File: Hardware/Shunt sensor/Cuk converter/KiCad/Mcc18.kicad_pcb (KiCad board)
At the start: 2 copper layers, 199.1 x 107.2 mm, 60 parts, among them Q1 IRFP4321PbF, U1 INA240, U2 DRIVER_(INEP), U3 LM7812_TO220, U4 Signals_MCC, U5 ZCS, U6 INA211_DCK_6

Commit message: finished the first version
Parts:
- removed C_INA211, C_INA240: 100n, MCCplaca:C_0805_2012Metric_Pad1.29x1.40mm_HandSolder
- removed RShunt1: R, MCCplaca Shunt:PML100HZPJV0L5
- removed R_Ina211_Ref1, R_Ina211_SIG1, R_Ina240_REF1, R_Ina240_SIG1: ??, MCCplaca Shunt:R_0805_2012Metric_Pad1.29x1.40mm_HandSolder
- added C1: 100nF, MCCplaca Shunt:C_0805_2012Metric_Pad1.29x1.40mm_HandSolder, B.Cu at (100.8, 51.3)
- added C12: 100nF, MCCplaca Shunt:C_0805_2012Metric_Pad1.29x1.40mm_HandSolder, F.Cu at (119.1, 56.4)
- added R105: 0R, Jumper:SolderJumper-2_P1.3mm_Open_Pad1.0x1.5mm, F.Cu at (126.2, 64.3)
- added R106: 0R, Jumper:SolderJumper-2_P1.3mm_Open_Pad1.0x1.5mm, B.Cu at (115.6, 51.6)
- added R108: 0R, Jumper:SolderJumper-2_P1.3mm_Open_Pad1.0x1.5mm, B.Cu at (115.6, 49.0)
- added R109: ??, Resistor_SMD:R_0805_2012Metric_Pad1.29x1.40mm_HandSolder, B.Cu at (103.9, 50.3)
- added R110: ??, Resistor_SMD:R_0805_2012Metric_Pad1.29x1.40mm_HandSolder, B.Cu at (103.9, 52.6)
- added Rshunt1: 500uR, MCCplaca Shunt:PML100HZPJV0L5, B.Cu at (126.0, 56.6)
- C11: value 10uF -> 100nF; footprint MCCplaca:C_0805_2012Metric_Pad1.29x1.40mm_HandSolder -> MCCplaca Shunt:C_0805_2012Metric_Pad1.29x1.40mm_HandSolder; moved to B.Cu
- R107: value 1R -> 0R; footprint Resistor_SMD:R_0805_2012Metric_Pad1.29x1.40mm_HandSolder -> Jumper:SolderJumper-2_P1.3mm_Open_Pad1.0x1.5mm
- U6: value INA211_DCK_6 -> INA211; moved to B.Cu
- moved U6 42.0 mm to (118.9, 56.4)
- moved C11 40.9 mm to (136.7, 56.9)
- moved R107 29.9 mm to (126.2, 61.7)
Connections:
- net /Shunt+ renamed /Rs+
- C11 pad 2: /Ipanel_adc+ -> +5VA
- R107 pad 1: /Ipanel_SIG -> GNDA
- R107 pad 2: /Ipanel_adc+ -> /Ip_sen-
- U1 pad 2: GND -> GNDA
- U1 pad 3: /Ina240_REF -> GNDA
- U1 pad 4: Net-(U1-Pad4) -> GNDA
- U1 pad 5: Net-(R_Ina240_SIG1-Pad2) -> /INA240_OUT
- U1 pad 6: +5V -> +5VA
- U1 pad 7: /Ina240_REF -> GNDA
- U6 pad 1: Net-(R_Ina211_Ref1-Pad2) -> GNDA
- U6 pad 2: GND -> GNDA
- U6 pad 3: +5V -> +5VA
- U6 pad 6: Net-(R_Ina211_SIG1-Pad2) -> /INA211_OUT
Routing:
- net GNDA: track 47.7 -> 135.8 mm, vias 3 -> 10
- net +5VA: track 7.91 -> 82.1 mm, vias 0 -> 4
- net +5V: track 195.2 -> 139.7 mm, vias 3 -> 1
- net /Ip_sen-: track 0.00 -> 37.5 mm, vias 0 -> 1
- net /Ip_sen+: track 0.00 -> 35.9 mm, vias 0 -> 1
- net /Ipanel_SIG: track 34.1 -> 0.00 mm, vias 2 -> 0
- net /Ina240_REF: track 21.7 -> 0.00 mm, vias 2 -> 0
- net GND: track 271.8 -> 252.6 mm, vias 10 -> 7
- net /-Vp: track 121.6 -> 136.1 mm
- net /Rs+: track 18.9 -> 30.8 mm
- net /INA211_OUT: track 0.00 -> 11.7 mm, vias 0 -> 2
- net Net-(R_Ina240_SIG1-Pad2): track 11.1 -> 0.00 mm, vias 1 -> 0
- net /INA240_OUT: track 0.00 -> 10.4 mm, vias 0 -> 1
- net /Ipanel_adc+: track 5.45 -> 14.9 mm, vias 0 -> 2
- removed copper zone on B.Cu, net (none)
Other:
- net class INA added: clearance 0.3048, trace_width 0.3429, via_dia 0.9, via_drill 0.7
- rule trace_min: 0.508 -> 0.3429

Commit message: fixed clearance
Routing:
- net GNDA: track 135.8 -> 136.4 mm
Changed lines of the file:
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@@
     (thickness 1.6)
     (drawings 8)
-    (tracks 655)
+    (tracks 658)
     (zones 0)
     (modules 61)
@@
     (user_trace_width 9)
     (trace_clearance 0.3048)
-    (zone_clearance 0.3048)
+    (zone_clearance 1.27)
     (zone_45_only no)
     (trace_min 0.3429)
@@
   (segment (start 133.223 54.00804) (end 133.223 51.943) (width 0.508) (layer B.Cu) (net 25))
   (segment (start 133.223 51.943) (end 133.096 51.816) (width 0.508) (layer B.Cu) (net 25))
-  (via (at 130.556 61.633997) (size 1.7) (drill 0.6) (layers F.Cu B.Cu) (net 25))
-  (segment (start 130.556 62.23) (end 130.556 61.633997) (width 0.508) (layer F.Cu) (net 25))
-  (segment (start 131.953 60.236997) (end 131.953 59.40804) (width 0.508) (layer B.Cu) (net 25))
-  (segment (start 130.556 61.633997) (end 131.953 60.236997) (width 0.508) (layer B.Cu) (net 25))
-  (segment (start 131.826 60.363997) (end 130.556 61.633997) (width 0.508) (layer F.Cu) (net 25))
-  (segment (start 131.826 56.896) (end 131.826 60.363997) (width 0.508) (layer F.Cu) (net 25))
-  (segment (start 133.096 51.816) (end 133.096 55.626) (width 0.508) (layer F.Cu) (net 25))
-  (segment (start 133.096 55.626) (end 131.826 56.896) (width 0.508) (layer F.Cu) (net 25))
-  (segment (start 130.467997 61.722) (end 130.556 61.633997) (width 0.508) (layer F.Cu) (net 25))
-  (segment (start 126.888 61.722) (end 130.467997 61.722) (width 0.508) (layer F.Cu) (net 25))
   (via (at 98.806 50.292) (size 1.8) (drill 0.7) (layers F.Cu B.Cu) (net 25))
   (segment (start 101.1405 50.292) (end 99.314 50.292) (width 0.508) (layer B.Cu) (net 25))
@@
   (segment (start 116.22 49.022) (end 117.094 49.022) (width 0.508) (layer B.Cu) (net 25))
   (segment (start 117.094 49.022) (end 119.888 51.816) (width 0.508) (layer B.Cu) (net 25))
+  (via (at 131.445006 61.468) (size 1.7) (drill 0.6) (layers F.Cu B.Cu) (net 25))
+  (segment (start 131.953 60.960006) (end 131.445006 61.468) (width 0.508) (layer B.Cu) (net 25))
+  (segment (start 130.556 62.23) (end 131.318 61.468) (width 0.508) (layer F.Cu) (net 25))
+  (segment (start 131.953 59.40804) (end 131.953 60.960006) (width 0.508) (layer B.Cu) (net 25))
+  (segment (start 131.191006 61.722) (end 131.445006 61.468) (width 0.508) (layer F.Cu) (net 25))
+  (segment (start 126.888 61.722) (end 131.191006 61.722) (width 0.508) (layer F.Cu) (net 25))
+  (segment (start 131.318 61.468) (end 131.445006 61.468) (width 0.508) (layer F.Cu) (net 25))
+  (segment (start 131.953 60.960006) (end 131.445006 61.468) (width 0.508) (layer F.Cu) (net 25))
+  (segment (start 131.953 57.3405) (end 131.953 60.960006) (width 0.508) (layer F.Cu) (net 25))
+  (segment (start 133.1595 56.134) (end 131.953 57.3405) (width 0.508) (layer F.Cu) (net 25))
+  (segment (start 133.096 51.816) (end 133.1595 51.8795) (width 0.508) (layer F.Cu) (net 25))
+  (segment (start 133.1595 51.8795) (end 133.1595 56.134) (width 0.508) (layer F.Cu) (net 25))
   (segment (start 119.94515 57.037999) (end 120.3579 57.037999) (width 0.3429) (layer B.Cu) (net 26))
   (segment (start 118.1585 56.388) (end 118.1585 56.4365) (width 0.3429) (layer F.Cu) (net 26))
@@
   (segment (start 114.3 62.738) (end 115.316 63.754) (width 0.508) (layer F.Cu) (net 60))
   (segment (start 115.316 63.754) (end 125.42521 63.754) (width 0.508) (layer F.Cu) (net 60))
-  (via (at 130.302 64.262) (size 1.7) (drill 0.6) (layers F.Cu B.Cu) (net 61))
-  (segment (start 126.888 64.262) (end 130.302 64.262) (width 0.508) (layer F.Cu) (net 61))
-  (segment (start 134.493 60.69104) (end 134.493 59.40804) (width 0.508) (layer B.Cu) (net 61))
-  (segment (start 130.302 64.262) (end 130.92204 64.262) (width 0.508) (layer B.Cu) (net 61))
-  (segment (start 130.92204 64.262) (end 134.493 60.69104) (width 0.508) (layer B.Cu) (net 61))
+  (via (at 131.445 64.0715) (size 1.7) (drill 0.6) (layers F.Cu B.Cu) (net 61))
+  (segment (start 126.888 64.262) (end 131.2545 64.262) (width 0.508) (layer F.Cu) (net 61))
+  (segment (start 131.2545 64.262) (end 131.445 64.0715) (width 0.508) (layer F.Cu) (net 61))
+  (segment (start 134.493 59.40804) (end 134.493 61.0235) (width 0.508) (layer B.Cu) (net 61))
+  (segment (start 134.493 61.0235) (end 132.294999 63.221501) (width 0.508) (layer B.Cu) (net 61))
+  (segment (start 132.294999 63.221501) (end 131.445 64.0715) (width 0.508) (layer B.Cu) (net 61))
   (via (at 117.856 54.356002) (size 1.5) (drill 0.6) (layers F.Cu B.Cu) (net 62))
   (segment (start 117.8941 54.394102) (end 117.856 54.356002) (width 0.3429) (layer B.Cu) (net 62))
@@
   )
   (zone (net 63) (net_name /Rs+) (layer B.Cu) (hatch full 0.508)
-    (priority 26)
-    (connect_pads yes (clearance 0.3048))
-    (min_thickness 0.254)
+    (priority 6)
+    (connect_pads yes (clearance 1.27))
+    (min_thickness 0.508)
     (fill yes (arc_segments 16) (thermal_gap 0.3048) (thermal_bridge_width 0.3048) (smoothing fillet) (radius 2))
     (polygon
@@
   )
   (zone (net 25) (net_name GNDA) (layer B.Cu) (hatch full 0.508)
-    (priority 25)
+    (priority 5)
     (connect_pads yes (clearance 0.3048))
     (min_thickness 0.508)
@@
   )
   (zone (net 25) (net_name GNDA) (layer F.Cu) (hatch full 0.508)
-    (priority 25)
+    (priority 5)
     (connect_pads yes (clearance 0.3048))
     (min_thickness 0.508)
@@
   )
   (zone (net 46) (net_name /-Vp) (layer B.Cu) (hatch edge 0.508)
-    (priority 3)
+    (priority 6)
     (connect_pads yes (clearance 1.27))
     (min_thickness 0.508)
-    (fill yes (arc_segments 16) (thermal_gap 0.508) (thermal_bridge_width 0.508) (smoothing fillet) (radius 4))
+    (fill yes (arc_segments 16) (thermal_gap 0.508) (thermal_bridge_width 0.508) (smoothing chamfer) (radius 3.81))
     (polygon
       (pts
@@
       )
     )
+  )
+  (zone (net 0) (net_name "") (layer B.Cu) (hatch full 0.508)
+    (connect_pads yes (clearance 0.3048))
+    (min_thickness 0.508)
+    (keepout (tracks allowed) (vias allowed) (copperpour not_allowed))
+    (fill (arc_segments 16) (thermal_gap 0.508) (thermal_bridge_width 0.508) (smoothing chamfer) (radius 2))
+    (polygon
+      (pts
+        (xy 129.4765 55.8165) (xy 129.4765 56.261) (xy 129.4765 57.2135) (xy 129.4765 57.404) (xy 129.4765 57.4675)
+        (xy 122.682 57.4675) (xy 122.682 57.15) (xy 122.682 56.3245) (xy 122.682 55.8165)
+      )
+    )

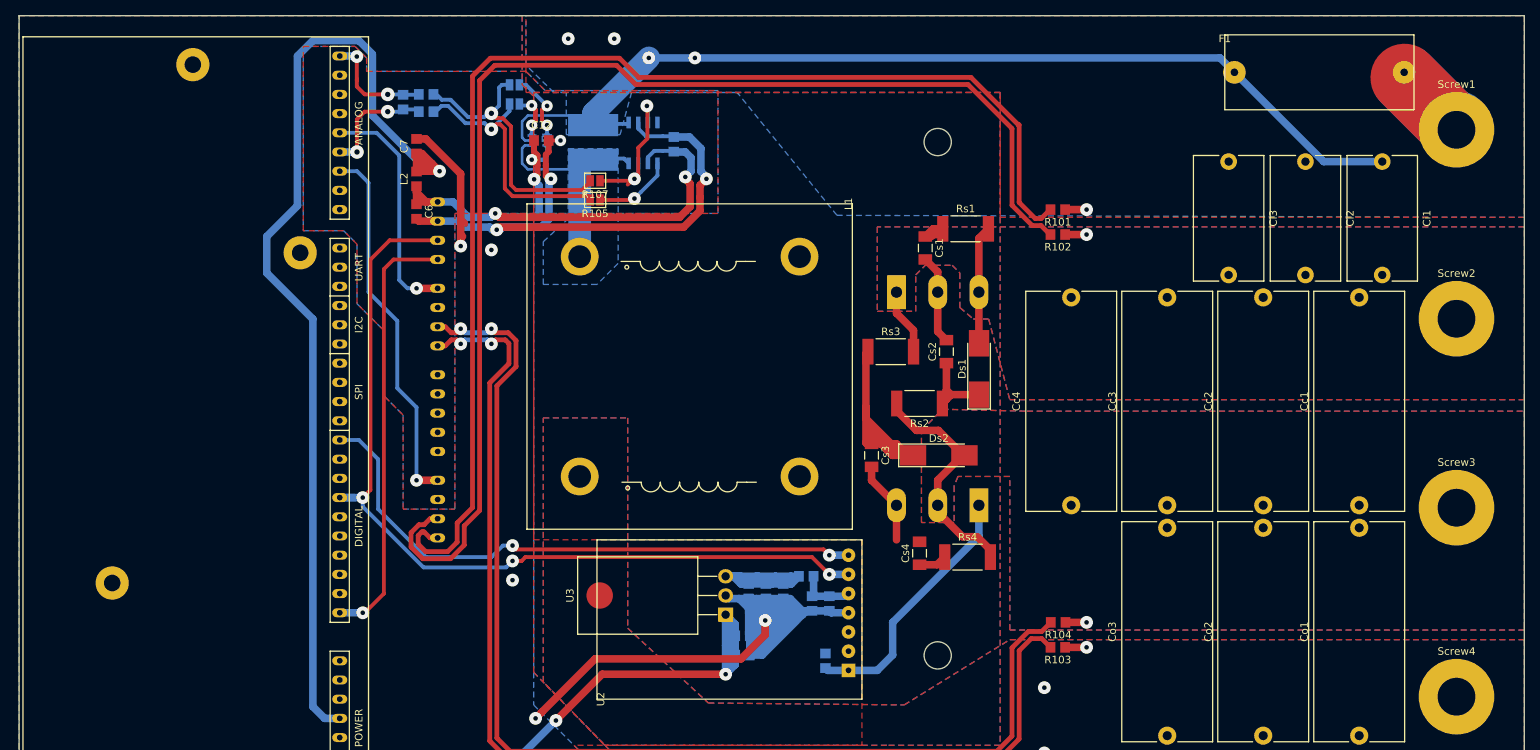
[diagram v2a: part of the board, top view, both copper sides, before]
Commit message: fixed shunt tracks and added 3d images
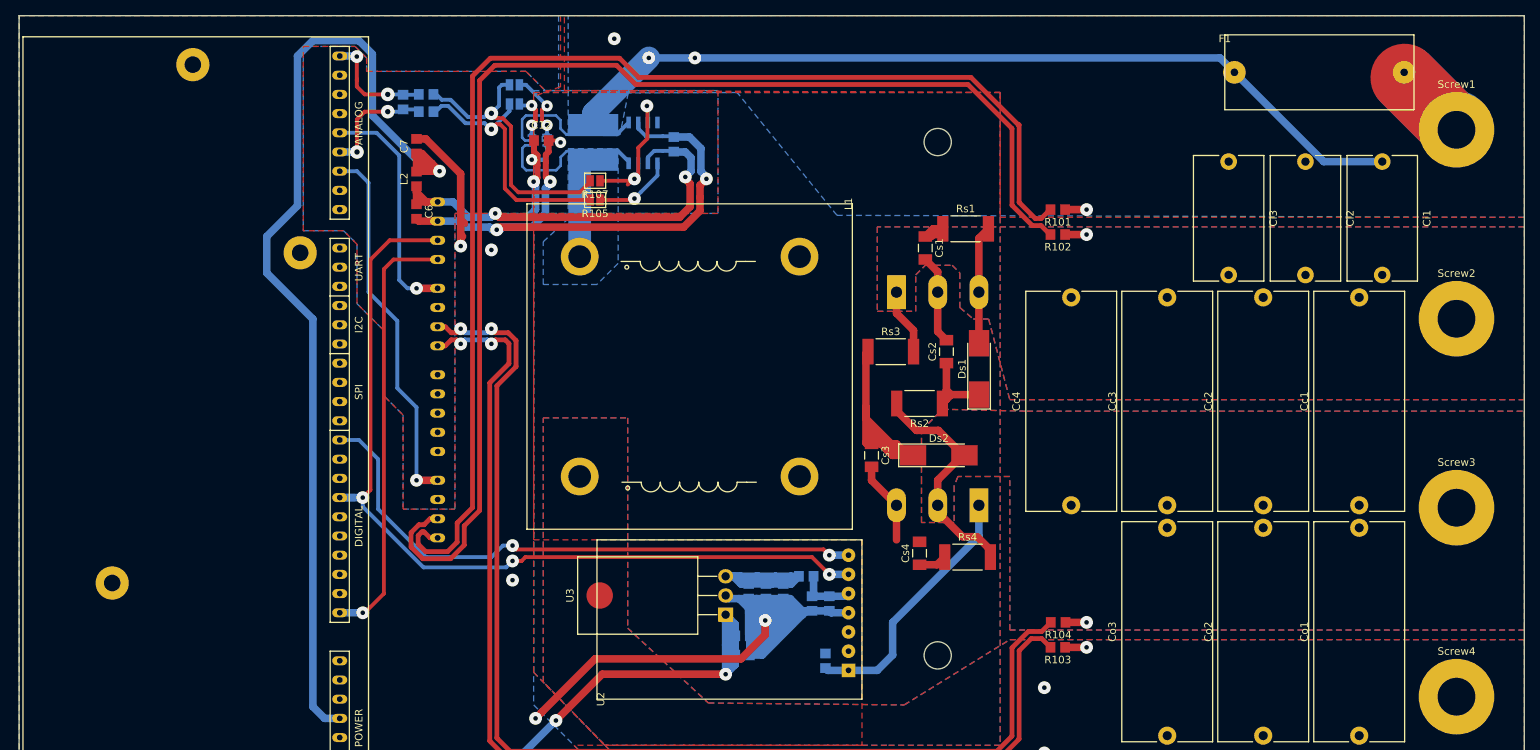
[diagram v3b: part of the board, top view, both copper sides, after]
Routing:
- net /-Vp: track 136.1 -> 146.4 mm, vias 5 -> 4
- net /Rs+: track 30.8 -> 37.4 mm
- net GNDA: track 136.4 -> 133.4 mm
- net +5VA: track 82.1 -> 80.5 mm

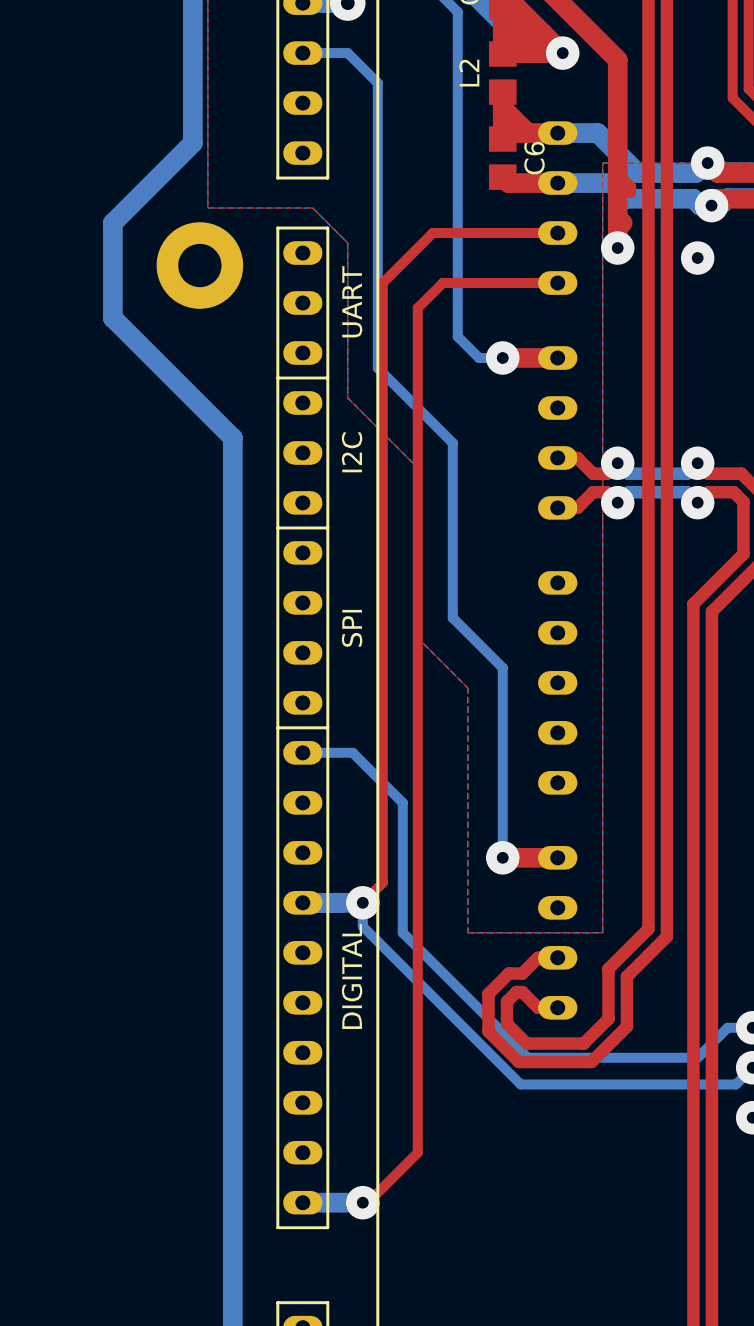
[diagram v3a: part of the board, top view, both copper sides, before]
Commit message: Added signals 3D in cuk PCB _Added signals 3D in signals component in MCCshunt Library._ _Added pin socket in the signals component_ _Added signals component in cuk converter PCB_ _Added MountingHoles to fix the signals PCB in thr cuk PCB_
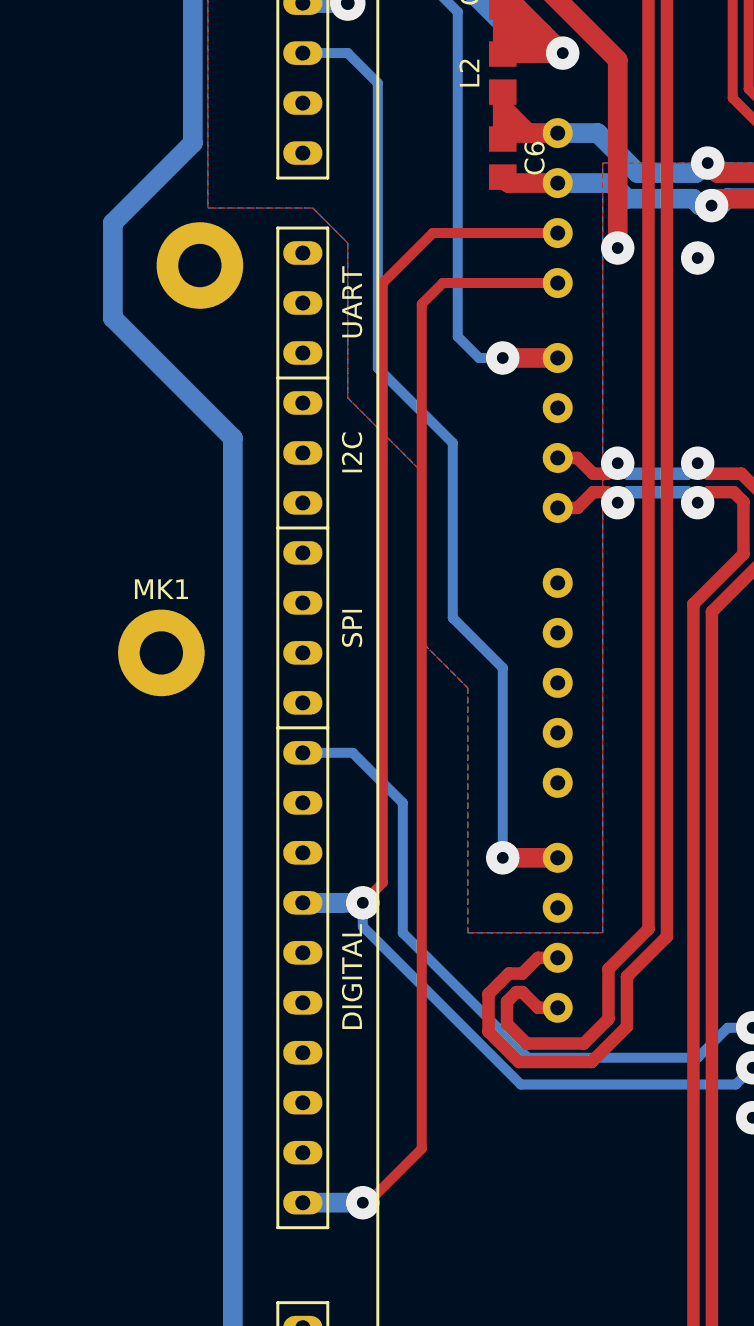
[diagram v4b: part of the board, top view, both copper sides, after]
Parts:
- added MK1: Mounting_Hole, MountingHole:MountingHole_2.2mm_M2_Pad, F.Cu at (85.3, 90.9)
- U4: footprint MCCplaca:Signals -> MCCplaca Shunt:Signals
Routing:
- net GND: track 252.6 -> 251.0 mm
